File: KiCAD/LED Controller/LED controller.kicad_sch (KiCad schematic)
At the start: 48 parts, among them J1 Barrel_Jack_Switch, J2 4x RJ45, J3 Conn_01x24_Female, J4 Conn_01x24_Female, J5 8P8C_Shielded, J6 Conn_01x03_Socket, J7 Conn_01x02_Socket, SW1 ELUMOASAQ2C22, SW2 ELUMOASAQ2C22, SW3 ELUMOASAQ2C22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

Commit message: CAD model for LED setup
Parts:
- H1, H2, H3, H4: now in the parts list
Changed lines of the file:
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@@
 		(unit 1)
 		(exclude_from_sim yes)
-		(in_bom no)
+		(in_bom yes)
 		(on_board yes)
 		(dnp no)
@@
 		(unit 1)
 		(exclude_from_sim yes)
-		(in_bom no)
+		(in_bom yes)
 		(on_board yes)
 		(dnp no)
@@
 		(unit 1)
 		(exclude_from_sim yes)
-		(in_bom no)
+		(in_bom yes)
 		(on_board yes)
 		(dnp no)
@@
 		(unit 1)
 		(exclude_from_sim yes)
-		(in_bom no)
+		(in_bom yes)
 		(on_board yes)
 		(dnp no)

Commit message: Change level shifter IC
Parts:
- U7: Manufacturer Nexperia USA Inc. -> Texas Instruments; Part NXB0104PWJ -> TXU0104PWR
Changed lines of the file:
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@@
 			)
 		)
-		(property "Datasheet" "https://assets.nexperia.com/documents/data-sheet/NXB0104.pdf"
+		(property "Datasheet" "https://www.ti.com/lit/ds/symlink/txu0104.pdf"
 			(at 97.282 150.368 0)
 			(effects
@@
 			)
 		)
-		(property "Description" "IC TRANSLATOR BIDIR 14TSSOP"
+		(property "Description" "IC TRANSLATOR UNIDIR 14TSSOP"
 			(at 109.22 162.56 0)
 			(effects
@@
 			)
 		)
-		(property "Manufacturer" "Nexperia USA Inc."
+		(property "Manufacturer" "Texas Instruments"
 			(at 123.825 157.2725 0)
 			(effects
@@
 			)
 		)
-		(property "Part" "NXB0104PWJ"
+		(property "Part" "TXU0104PWR"
 			(at 123.825 159.6968 0)
 			(effects
@@
 			)
 		)
-		(property "Part #" ""
-			(at 109.22 162.56 0)
-			(effects
-				(font
-					(size 1.27 1.27)
-				)
-				(hide yes)
-			)
-		)
 		(pin "13"
 		)
@@
 	)
 	(symbol
-		(lib_name "Custom_parts:Conn_01x24_Female")
 		(lib_id "Custom_parts:Conn_01x24_Female")
 		(at 182.88 68.58 0)
@@
 	)
 	(symbol
-		(lib_name "Custom_parts:Conn_01x24_Female")
 		(lib_id "Custom_parts:Conn_01x24_Female")
 		(at 271.78 68.58 0)

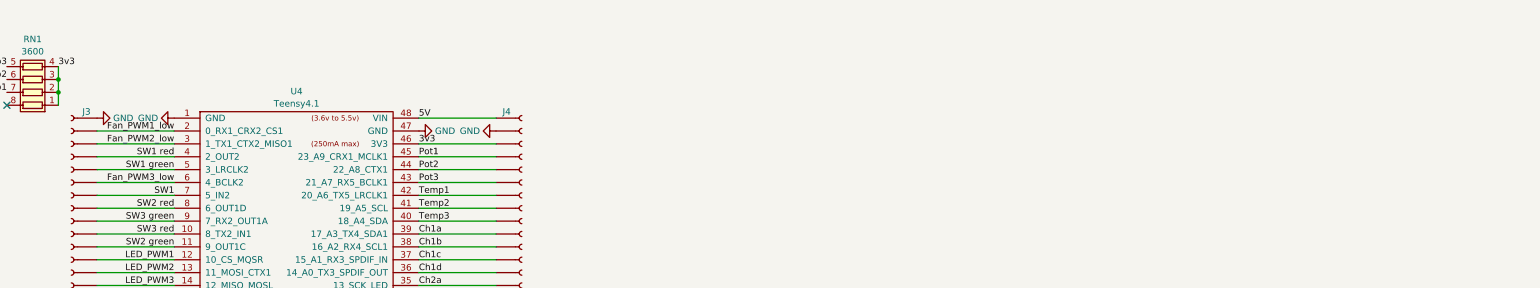
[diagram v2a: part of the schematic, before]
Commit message: Add notes for revision to controller board
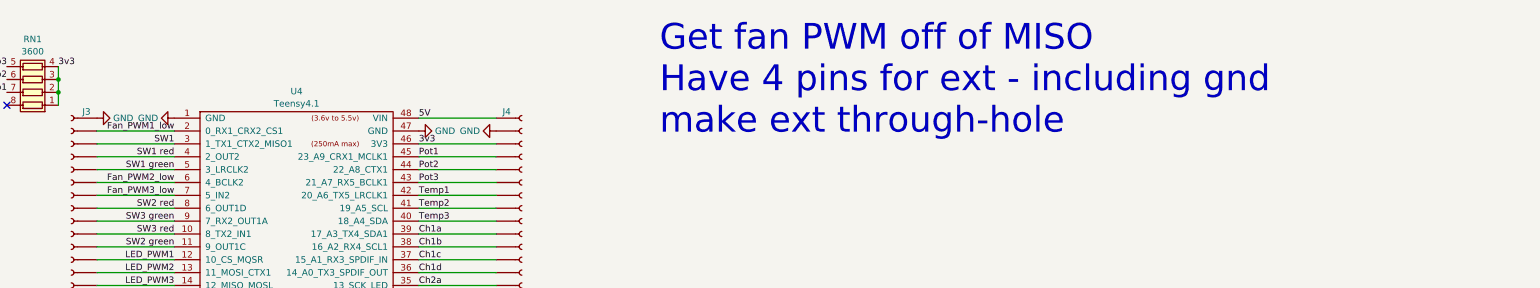
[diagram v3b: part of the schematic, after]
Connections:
- net Fan_PWM2_low: now also U4.6 (4_BCLK2); no longer U4.3 (1_TX1_CTX2_MISO1)
- net Fan_PWM3_low: now also U4.7 (5_IN2); no longer U4.6 (4_BCLK2)
- net SW1: now also U4.3 (1_TX1_CTX2_MISO1); no longer U4.7 (5_IN2)
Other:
- note added: "Get fan PWM off of MISO Have 4 pins for ext - including gnd make ext through-hole"
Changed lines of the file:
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@@
 		)
 	)
+	(text "Get fan PWM off of MISO\nHave 4 pins for ext - including gnd\nmake ext through-hole"
+		(exclude_from_sim no)
+		(at 298.958 33.02 0)
+		(effects
+			(font
+				(size 5.08 5.08)
+			)
+			(justify left)
+		)
+	)
 	(label "SDA"
 		(at 157.48 128.27 180)
@@
 	)
 	(label "Fan_PWM3_low"
-		(at 203.2 53.34 180)
+		(at 203.2 55.88 180)
 		(fields_autoplaced yes)
 		(effects
@@
 	)
 	(label "Fan_PWM2_low"
-		(at 203.2 45.72 180)
+		(at 203.2 53.34 180)
 		(fields_autoplaced yes)
 		(effects
@@
 	)
 	(label "SW1"
-		(at 203.2 55.88 180)
+		(at 203.2 45.72 180)
 		(fields_autoplaced yes)
 		(effects
@@
 			)
 		)
-		(property "Datasheet" "https://mspindy.com/technical-guides/transducers-external-drive-piezo/"
+		(property "Datasheet" "https://www.mouser.com/datasheet/2/252/PT_2745WQ-3220810.pdf"
 			(at 158.496 135.89 0)
 			(effects
